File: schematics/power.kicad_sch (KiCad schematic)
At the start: 30 parts, among them IC1 RT6150BGQW, J4 LiPo, J5 TYPE-C-31-M-12, Q2 Q_PMOS_GSD, SW3 PWROFF_Switch, U4 U3V40F6, U5 MCP73831T-2ACI_OT

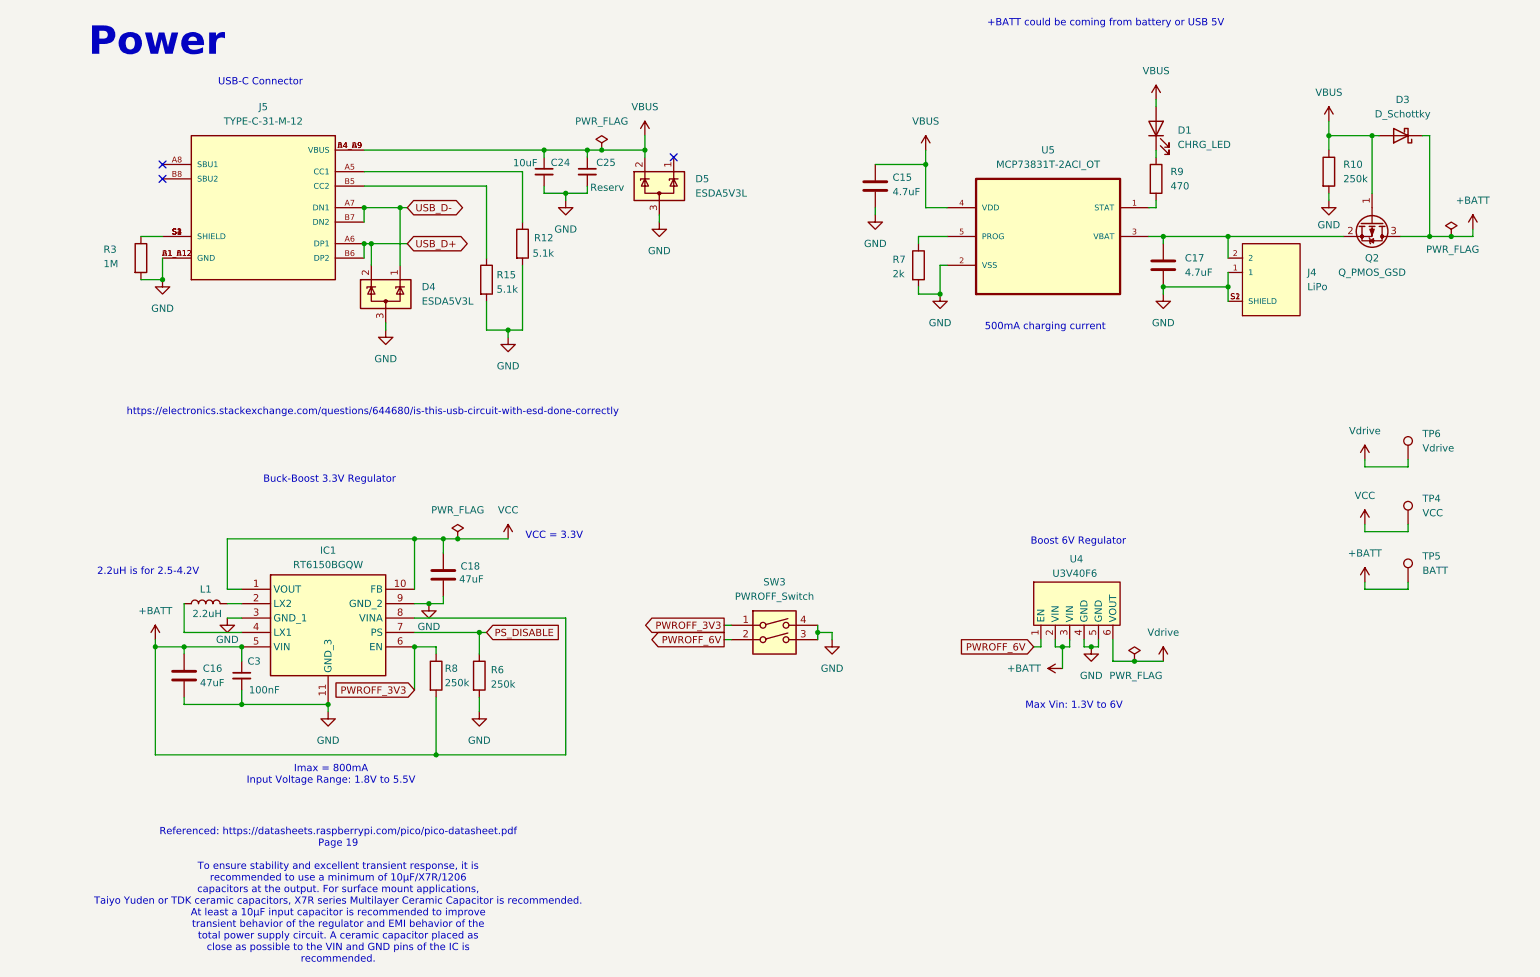
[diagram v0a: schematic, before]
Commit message: Fixed mistake in battery bypass circuit.
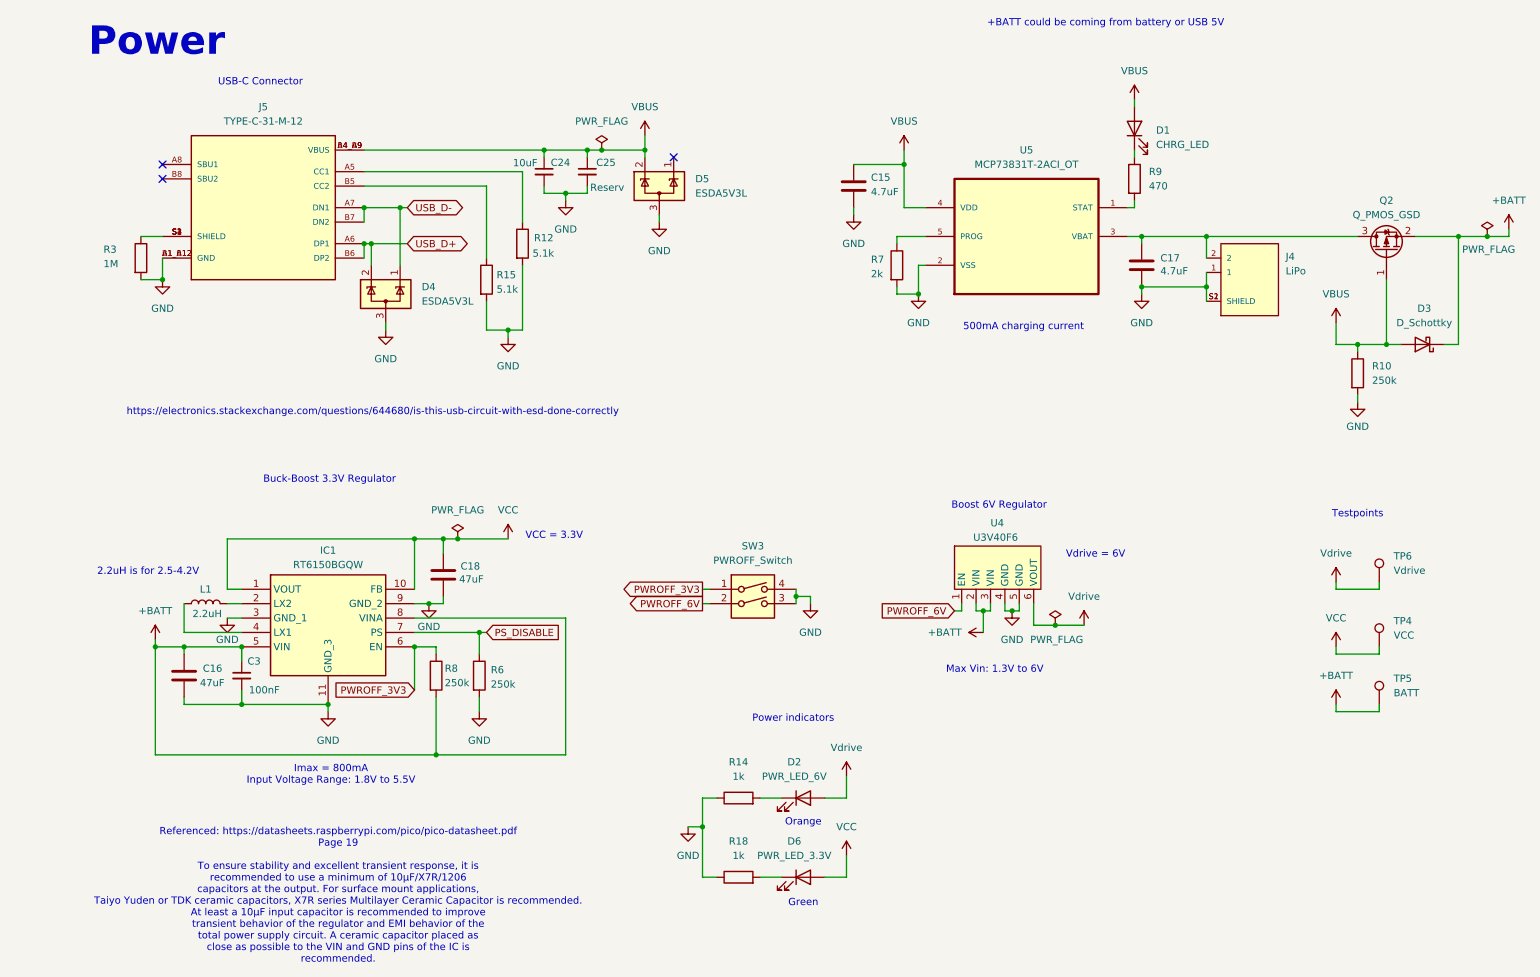
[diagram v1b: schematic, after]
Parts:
- added D2: PWR_LED_6V, LED_SMD:LED_0805_2012Metric_Pad1.15x1.40mm_HandSolder, symbol Device:LED
- added D6: PWR_LED_3.3V, LED_SMD:LED_0805_2012Metric_Pad1.15x1.40mm_HandSolder, symbol Device:LED
- added R14, R18: 1k, Resistor_SMD:R_0603_1608Metric_Pad0.98x0.95mm_HandSolder, symbol Device:R
- C16, C18: footprint Capacitor_Tantalum_SMD:CP_EIA-3216-18_Kemet-A_Pad1.58x1.35mm_HandSolder -> Capacitor_SMD:C_1210_3225Metric_Pad1.33x2.70mm_HandSolder
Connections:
- net +BATT: now also Q2.2 (S); no longer Q2.3 (D)
- net GND: now also R14.1, R18.1
- net VCC: now also D6.2 (A)
- net Vdrive: now also D2.2 (A)
- net at C17.1, J4.2, U5.3 (VBAT): now also Q2.3 (D); no longer Q2.2 (S)
- new net: D2.1 (K), R14.2
- new net: D6.1 (K), R18.2
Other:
- note added: "Green"
- note added: "Orange"
- note added: "Power indicators"
- note added: "Testpoints"
- note added: "Vdrive = 6V"
- moved on the sheet: C15, C17, D1, D3, J4, Q2, R10, R7, R9, SW3, TP4, TP5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
